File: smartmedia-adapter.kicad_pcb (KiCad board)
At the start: 2 copper layers, 37 x 45 mm, 2 parts, among them T1 SmartMedia_Normal, U1 XD_Card

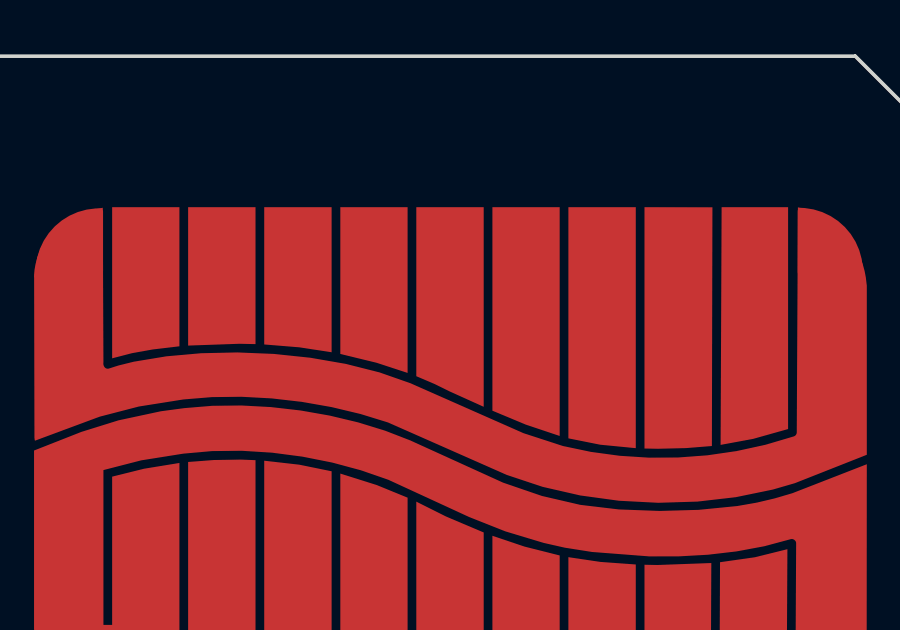
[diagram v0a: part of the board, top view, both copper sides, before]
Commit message: update footprints to be more accurate
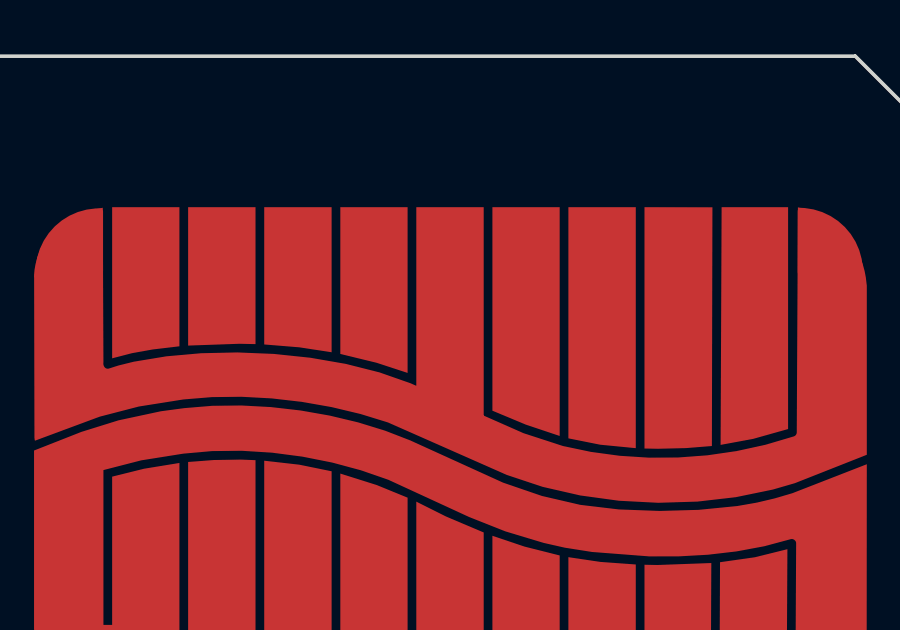
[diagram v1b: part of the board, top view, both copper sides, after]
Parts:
- T1: footprint Library:Smartmedia card rwar1 -> Library:Smartmedia card 3.3v
- U1: footprint Library:tempthing -> Library:XD_card
